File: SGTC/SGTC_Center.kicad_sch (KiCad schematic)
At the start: 32 parts, among them J10 Conn_01x04_Pin, J11 Conn_01x04_Pin, J2 Conn_01x01_Pin, J3 Conn_01x03_Pin, J4 Conn_01x01_Pin, J5 Conn_01x01_Pin, J6 Conn_01x01_Pin, J7 Conn_01x01_Pin, J8 Conn_01x01_Pin, J9 Conn_01x01_Pin, U1 ADS131M03QPWRQ1, U2 TMP235A4DBZR

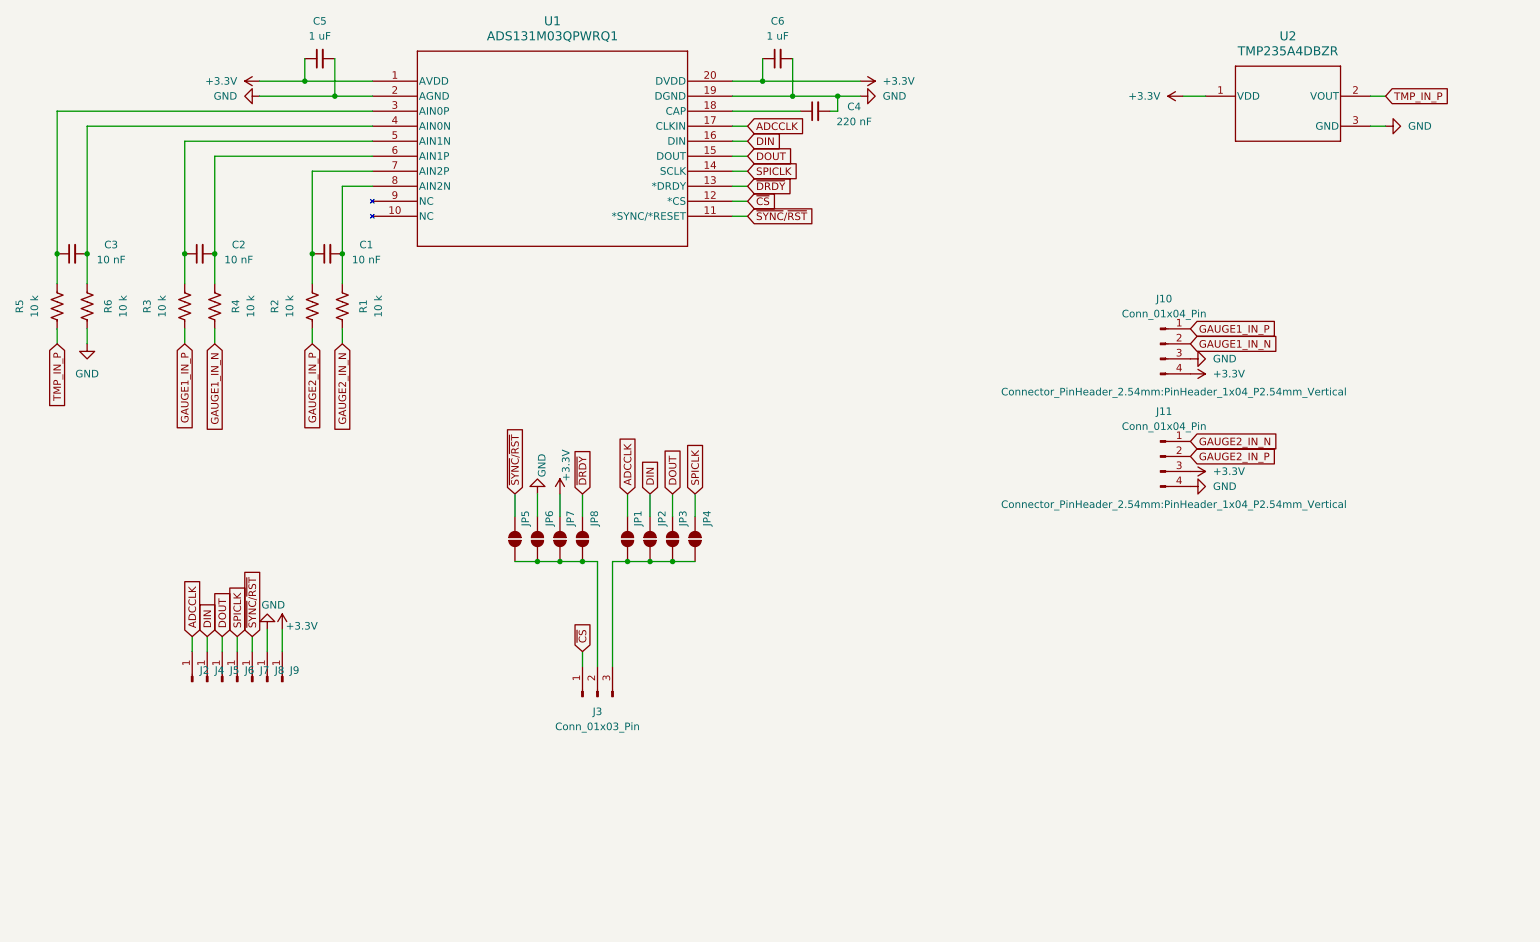
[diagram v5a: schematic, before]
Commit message: update fins with bridge completion resistors
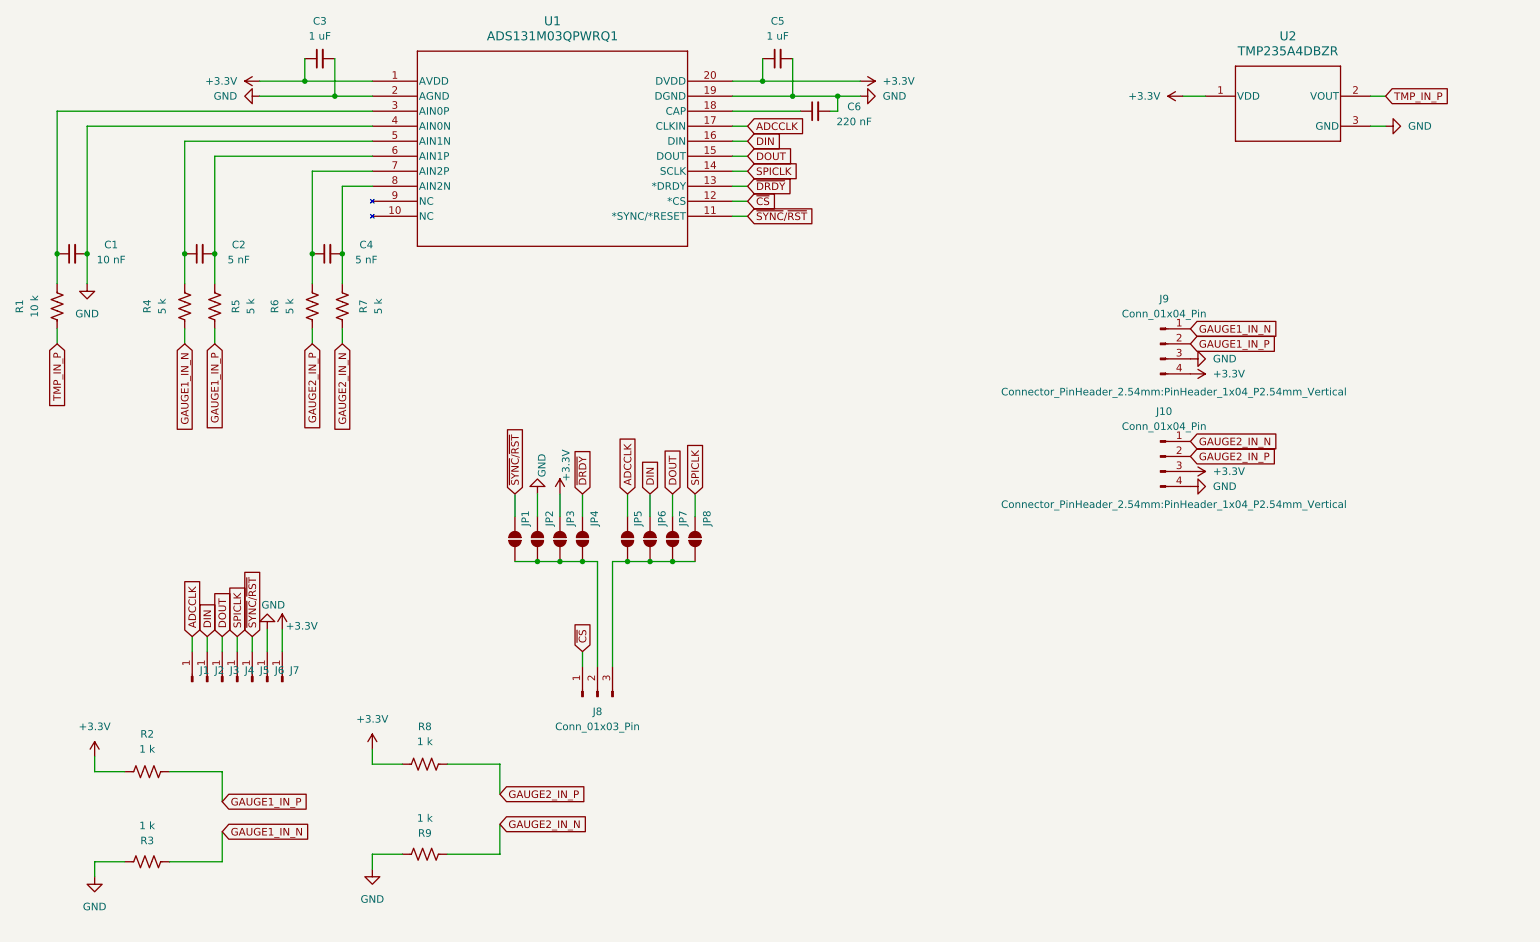
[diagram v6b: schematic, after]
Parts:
- added R2, R8, R9: 1 k, Resistor_SMD:R_0603_1608Metric, symbol Device:R_US
- C2: value 10 nF -> 5 nF
- C4: renamed from C1; value 10 nF -> 5 nF
- R3: renamed from R6; value 10 k -> 1 k
- R4: renamed from R3; value 10 k -> 5 k
- R5: renamed from R4; value 10 k -> 5 k
- R6: renamed from R2; value 10 k -> 5 k
- R7: renamed from R1; value 10 k -> 5 k
- renumbered C3 to C1, C5 to C3, C6 to C5, C4 to C6, J2 to J1, J11 to J10, J4 to J2, J5 to J3, J6 to J4, J7 to J5, J8 to J6, J9 to J7, J3 to J8, J10 to J9, JP5 to JP1, JP6 to JP2, JP7 to JP3, JP8 to JP4, JP1 to JP5, JP2 to JP6, JP3 to JP7, JP4 to JP8, R5 to R1
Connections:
- net +3.3V: now also R2.1, R8.1
- net GAUGE1_IN_N: now also J9.1 (Pin_1), R3.2, R4.1; no longer J9.2 (Pin_2), R5.2
- net GAUGE1_IN_P: now also J9.2 (Pin_2), R5.2, R2.2; no longer J9.1 (Pin_1), R4.1
- net GAUGE2_IN_N: now also R9.2
- net GAUGE2_IN_P: now also R8.2
- net GND: now also C1.2, R3.1, U1.4 (AIN0N), R9.1; no longer R3.2
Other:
- moved on the sheet: R3

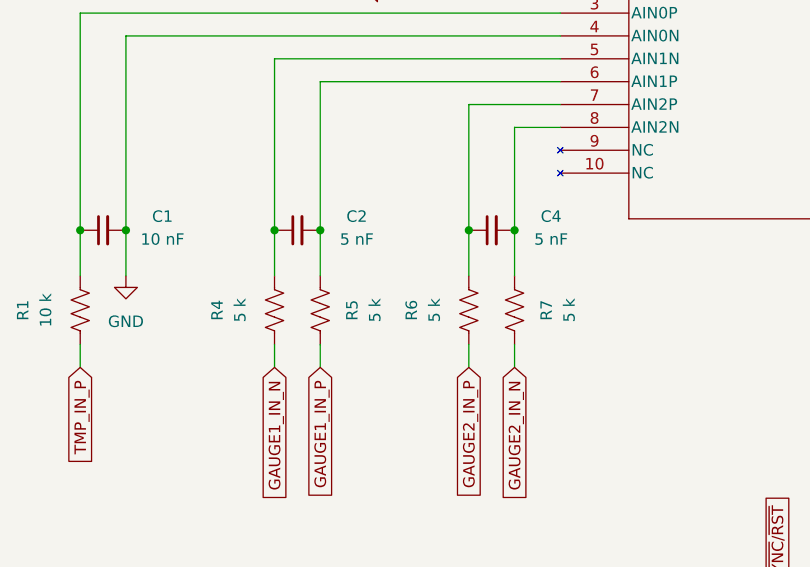
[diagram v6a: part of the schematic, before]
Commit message: update RC filter values
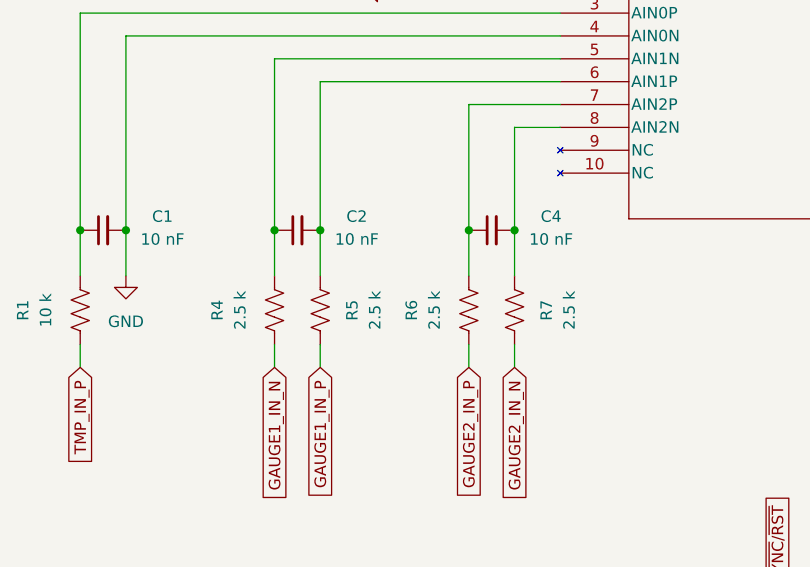
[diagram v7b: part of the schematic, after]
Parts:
- C2, C4: value 5 nF -> 10 nF
- R4, R5, R6, R7: value 5 k -> 2.5 k
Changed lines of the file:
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@@
 			)
 		)
-		(property "Value" "5 nF"
+		(property "Value" "10 nF"
 			(at 76.454 82.296 90)
 			(effects
@@
 			)
 		)
-		(property "Value" "5 nF"
+		(property "Value" "10 nF"
 			(at 54.864 82.296 90)
 			(effects
@@
 			)
 		)
-		(property "Value" "5 k"
+		(property "Value" "2.5 k"
 			(at 63.5 90.17 90)
 			(effects
@@
 			)
 		)
-		(property "Value" "5 k"
+		(property "Value" "2.5 k"
 			(at 56.896 90.17 90)
 			(effects
@@
 			)
 		)
-		(property "Value" "5 k"
+		(property "Value" "2.5 k"
 			(at 41.91 90.17 90)
 			(effects
@@
 			)
 		)
-		(property "Value" "5 k"
+		(property "Value" "2.5 k"
 			(at 78.486 90.17 90)
 			(effects

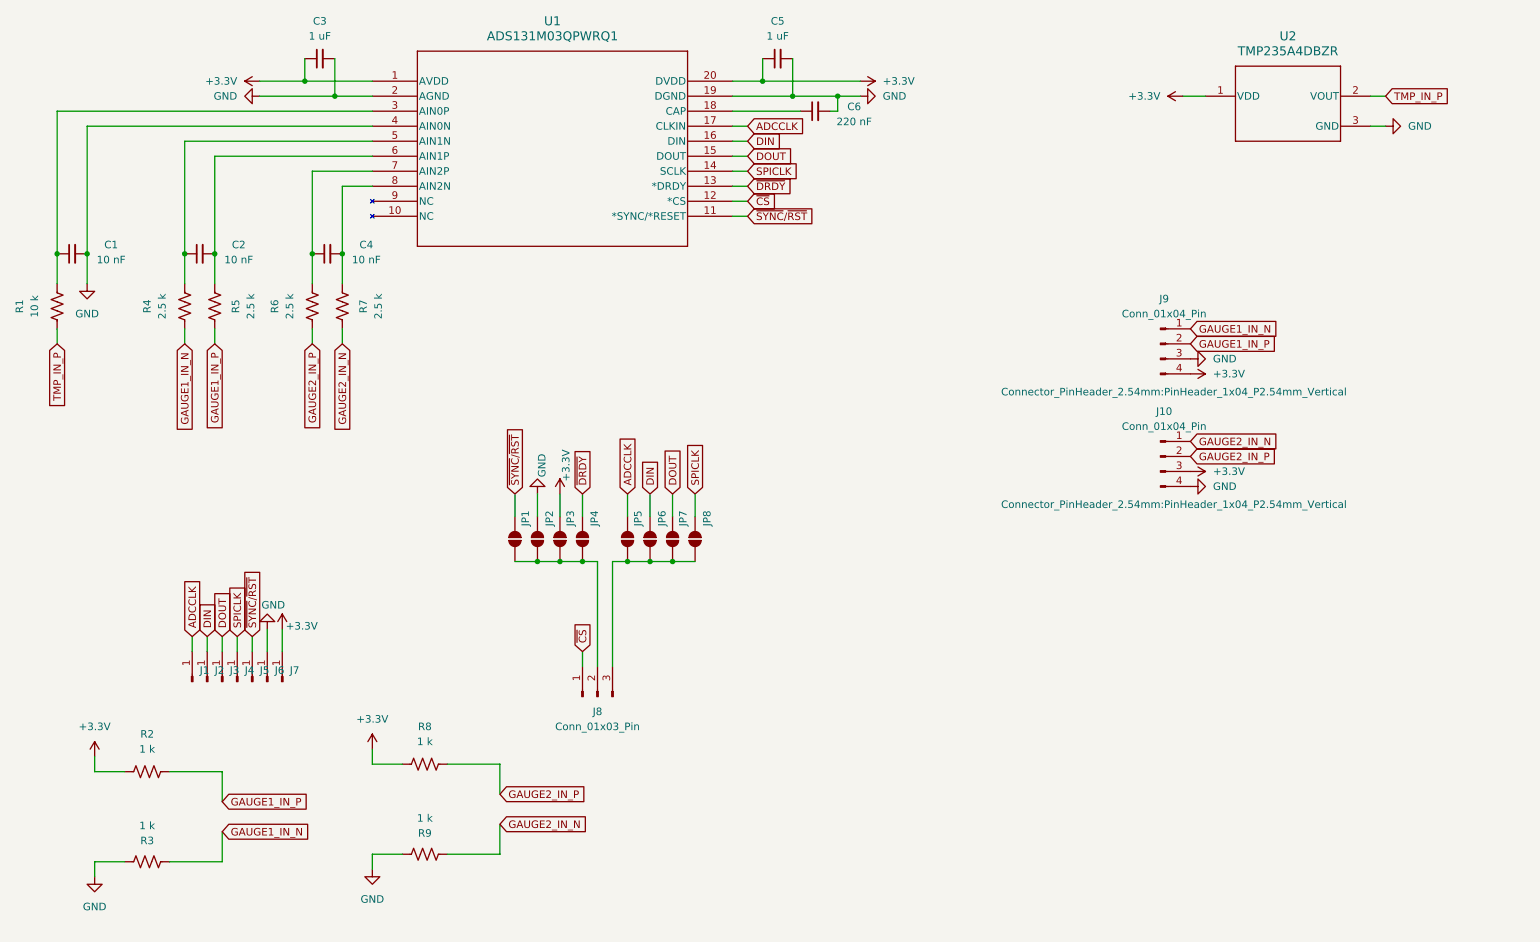
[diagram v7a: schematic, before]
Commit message: remake boards better with four layers
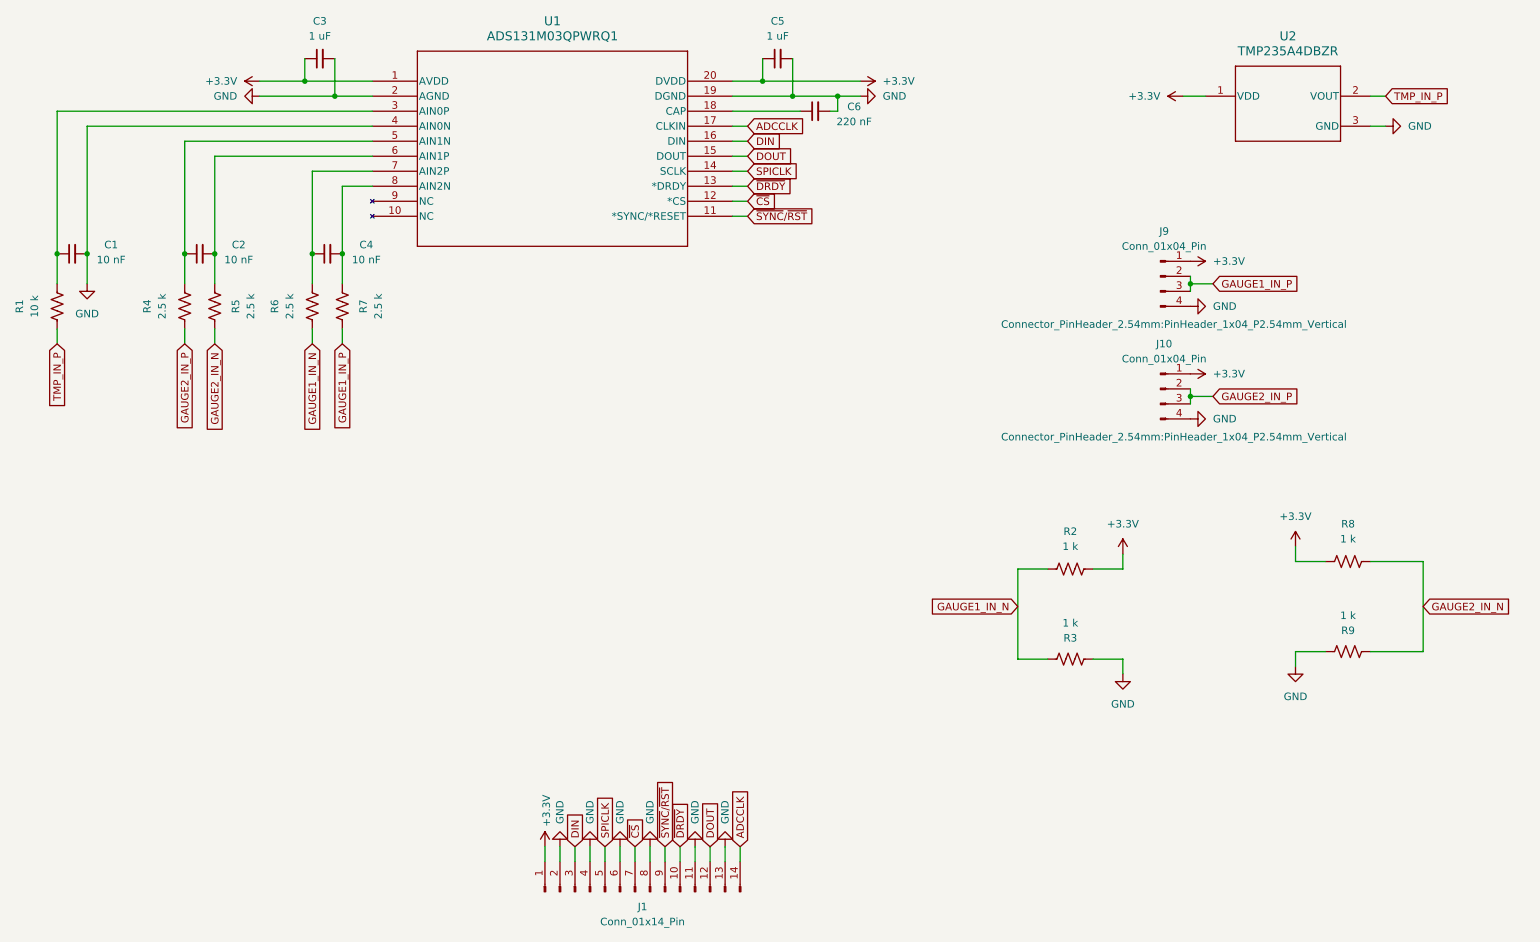
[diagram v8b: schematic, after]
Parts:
- removed J1, J2, J3, J4, J5, J6, J7: Conn_01x01_Pin, Connector_PinHeader_2.54mm:PinHeader_1x01_P2.54mm_Vertical, symbol Connector:Conn_01x01_Pin
- removed J8: Conn_01x03_Pin, Connector_PinHeader_2.54mm:PinHeader_1x03_P2.54mm_Vertical, symbol Connector:Conn_01x03_Pin
- removed JP1, JP2, JP3, JP4, JP5, JP6, JP7, JP8: SolderJumper_2_Open, Jumper:SolderJumper-2_P1.3mm_Open_RoundedPad1.0x1.5mm, symbol Jumper:SolderJumper_2_Open
- added J1: Conn_01x14_Pin, TerminalBlock_Phoenix:TerminalBlock_Phoenix_MKDS-1,5-14-5.08_1x14_P5.08mm_Horizontal, symbol Connector:Conn_01x14_Pin
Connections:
- net +3.3V: now also J10.1 (Pin_1), J9.1 (Pin_1), R2.2, J1.1 (Pin_1); no longer J10.3 (Pin_3), J9.4 (Pin_4), R2.1
- net ADCCLK: now also J1.14 (Pin_14)
- net DIN: now also J1.3 (Pin_3)
- net DOUT: now also J1.12 (Pin_12)
- net GAUGE1_IN_N: now also R2.1, R3.1, R6.1; no longer J9.1 (Pin_1), R3.2, R4.1
- net GAUGE1_IN_P: now also J9.3 (Pin_3), R7.2; no longer R2.2, R5.2
- net GAUGE2_IN_N: now also R5.2, R8.2; no longer J10.1 (Pin_1), R7.2
- net GAUGE2_IN_P: now also J10.3 (Pin_3), R4.1; no longer R6.1, R8.2
- net GND: now also J9.4 (Pin_4), R3.2, J1.11 (Pin_11), J1.13 (Pin_13), J1.2 (Pin_2), J1.4 (Pin_4), J1.6 (Pin_6), J1.8 (Pin_8); no longer J9.3 (Pin_3), R3.1
- net SPICLK: now also J1.5 (Pin_5)
- net ~{CS}: now also J1.7 (Pin_7)
- net ~{DRDY}: now also J1.10 (Pin_10)
- net ~{SYNC}/~{RST}: now also J1.9 (Pin_9)
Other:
- moved on the sheet: J10, J9, R2, R3, R8, R9
